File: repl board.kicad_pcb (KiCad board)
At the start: 2 copper layers, 55.5 x 32.2 mm, 24 parts, among them IC1 SN74HC42D, IC2 SN74HC42D, J2 Conn_01x16, J3 Conn_01x16, SW2 SW_Reed, U1 ATmega32U2-AU, Y1 ABM8G-16.000MHZ-4Y-T3

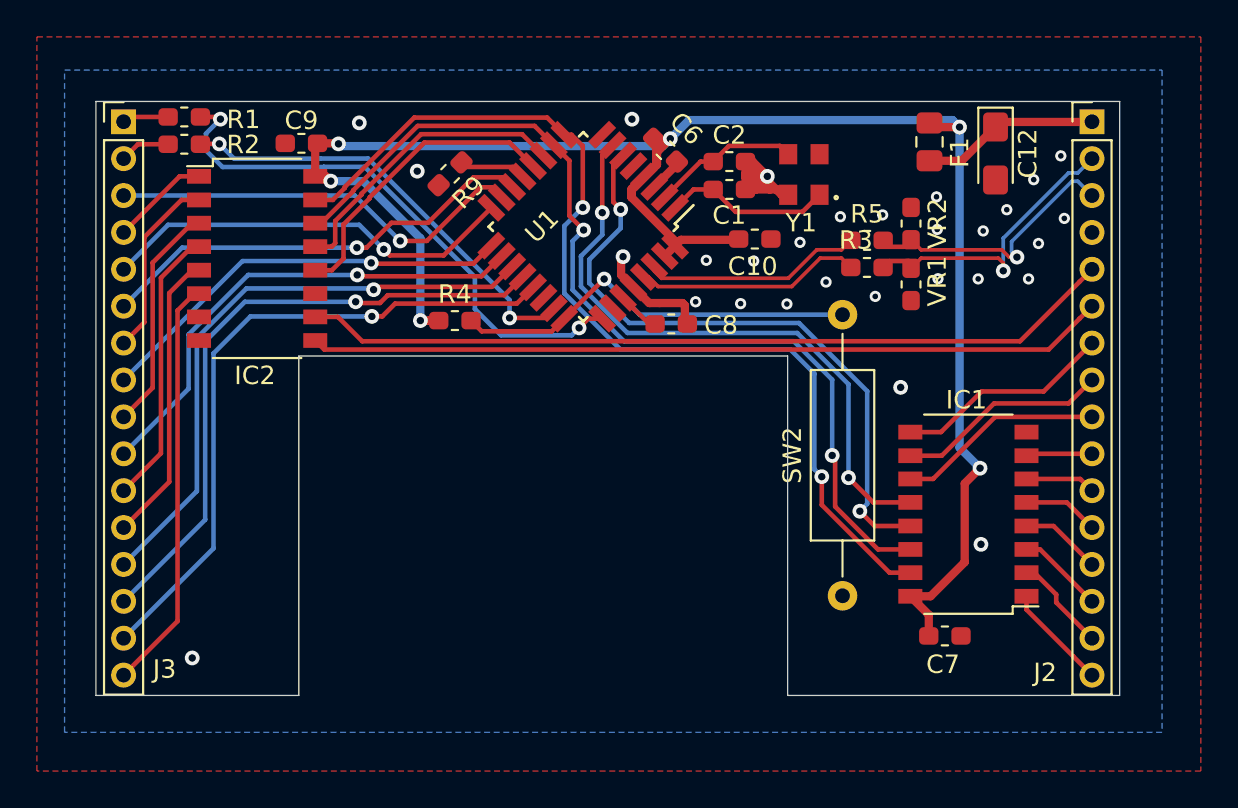
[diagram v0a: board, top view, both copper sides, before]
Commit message: Fix chrystal
Fix Chrystal footprint, added ICSP header
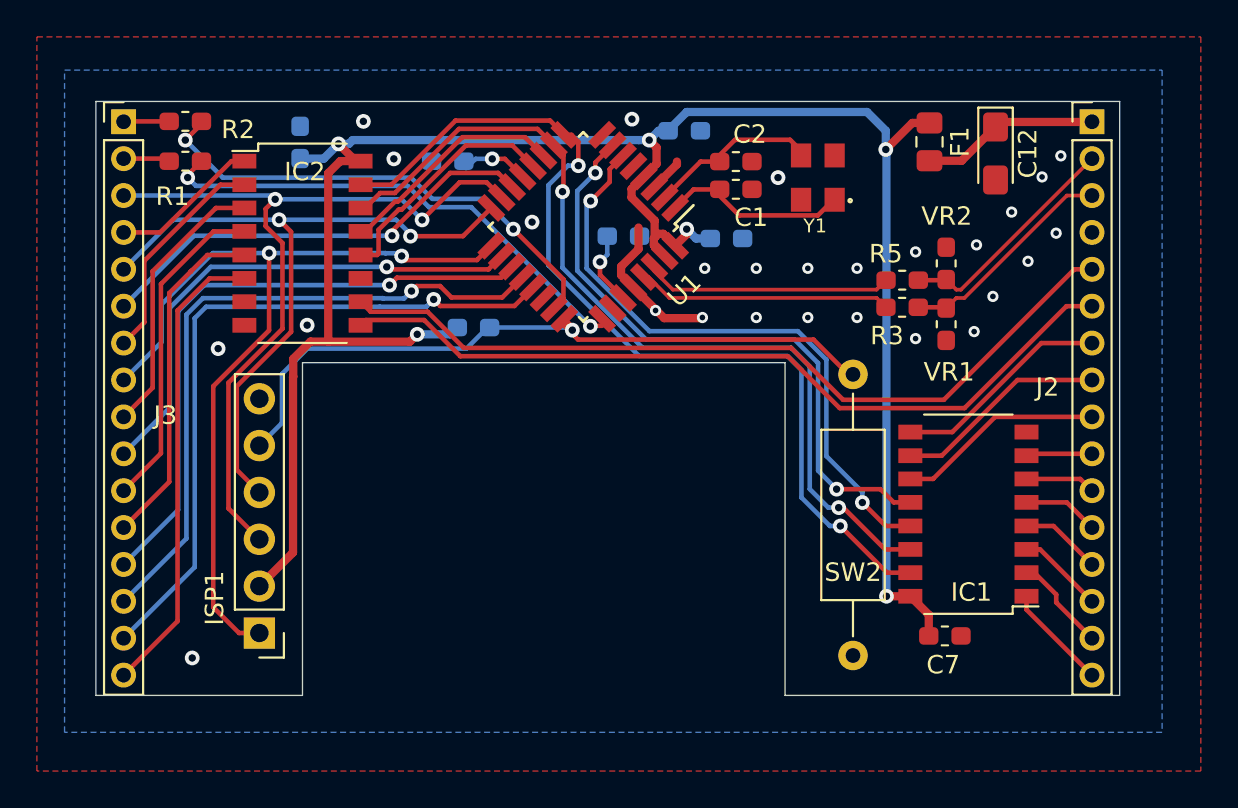
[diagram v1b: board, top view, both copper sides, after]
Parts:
- added ISP1: AVR-ISP-6, Connector_PinHeader_2.54mm:PinHeader_1x06_P2.54mm_Vertical, F.Cu at (172.2, 109.0)
- C10, C6, C8, C9, R4, R9: moved to B.Cu
- Y1: value ABM8G-16.000MHZ-4Y-T3 -> ABM8G-16MHZ-4Y-T3
- moved C8 5.42 mm to (191.9, 87.5)
- moved SW2 3.29 mm to (204.3, 110.2)
- moved VR2 2.88 mm to (209.4, 89.0)
- moved R3 2.88 mm to (207.0, 91.4)
- moved R5 2.88 mm to (207.0, 89.9)
- moved VR1 2.88 mm to (209.4, 92.3)
- moved IC2 2.59 mm to (174.5, 87.9)
- moved R1 2.40 mm to (168.1, 83.4)
- moved C10 1.54 mm to (197.5, 87.6)
- moved C6 1.46 mm to (195.2, 81.8), turned to 0 degrees
- moved R2 1.24 mm to (168.1, 81.3)
- moved R4 1.08 mm to (183.8, 92.5)
- moved Y1 0.78 mm to (202.4, 84.3)
- moved R9 0.69 mm to (182.4, 83.4), turned to 180 degrees
- moved C1 0.35 mm to (198.0, 85.0)
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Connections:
- net Net-(R4-Pad2) renamed Reset
- J2 pad 2: D+ -> D-
- J2 pad 3: D- -> D+
- J3 pad 1: CAP -> SCR
- J3 pad 2: SCR -> CAP
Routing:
- net COL3: track 23.1 -> 48.0 mm, vias 1 -> 2
- net COL1: track 23.0 -> 43.2 mm, vias 1 -> 2
- net Reset: track 22.4 -> 39.6 mm
- net COL2: track 22.7 -> 38.9 mm, vias 1 -> 2
- net VCC: track 99.8 -> 112.8 mm
- net GND: track 20.8 -> 10.1 mm, vias 29 -> 27
- net D+: track 16.1 -> 12.0 mm, vias 1 -> 0
- net ROWB: track 52.4 -> 48.6 mm
- net ROWE: track 16.1 -> 12.4 mm
- net ROWF: track 16.3 -> 13.0 mm
- net /LED_CAP: track 30.2 -> 27.0 mm
- net /LED_SCR: track 23.9 -> 26.8 mm
- net ROW14: track 15.9 -> 18.8 mm
- net ROW15: track 22.5 -> 25.3 mm
- net ROW10: track 5.35 -> 8.15 mm
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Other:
- outline, holes or cut-outs redrawn

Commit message: v1.05
Corrected USB D+/D-
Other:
- board text added: "Filco TKL Controller v1.05 2020 Markus Knutsson CERN-OHL-S v2+ github.com/TweetyDaBird/"
- board text removed: "2020 Markus Knutsson CERN-OHL-S v2+ github.com/TweetyDaBird/"

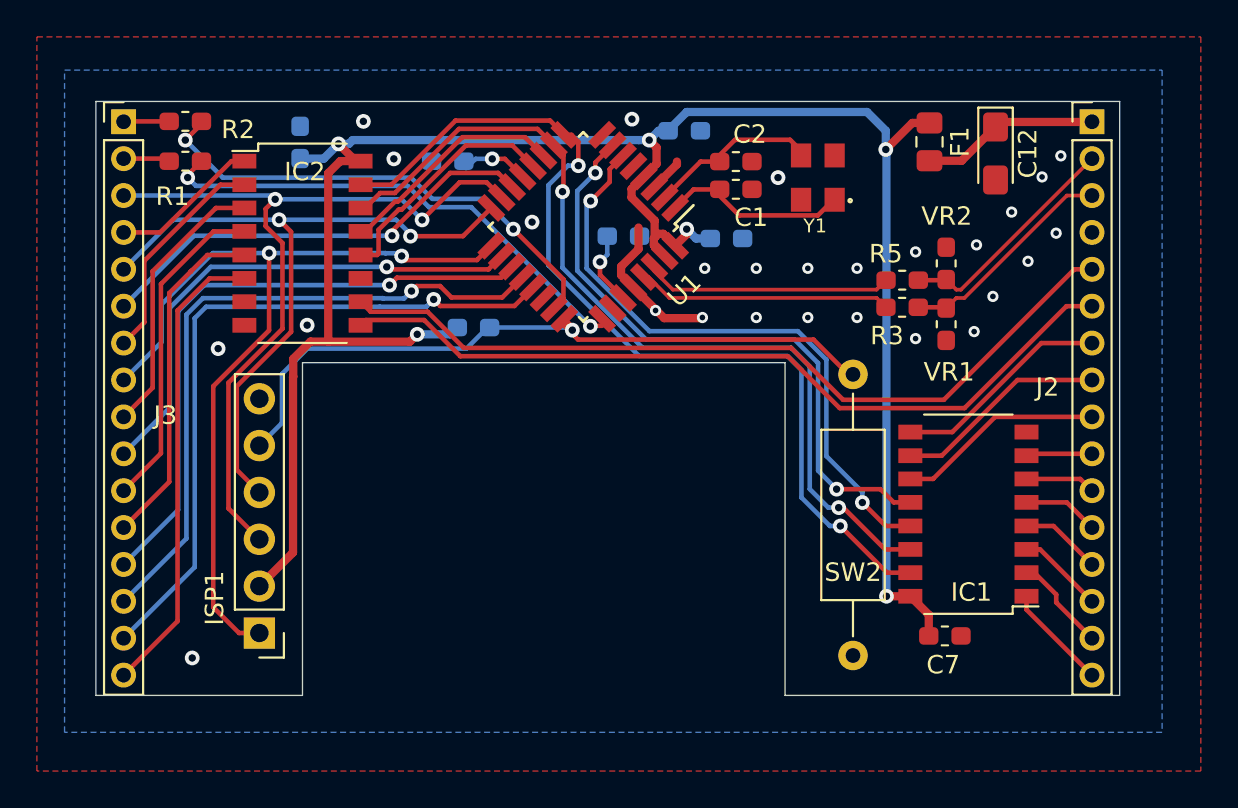
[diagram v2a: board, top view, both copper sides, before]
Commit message: Adjustment for DRC
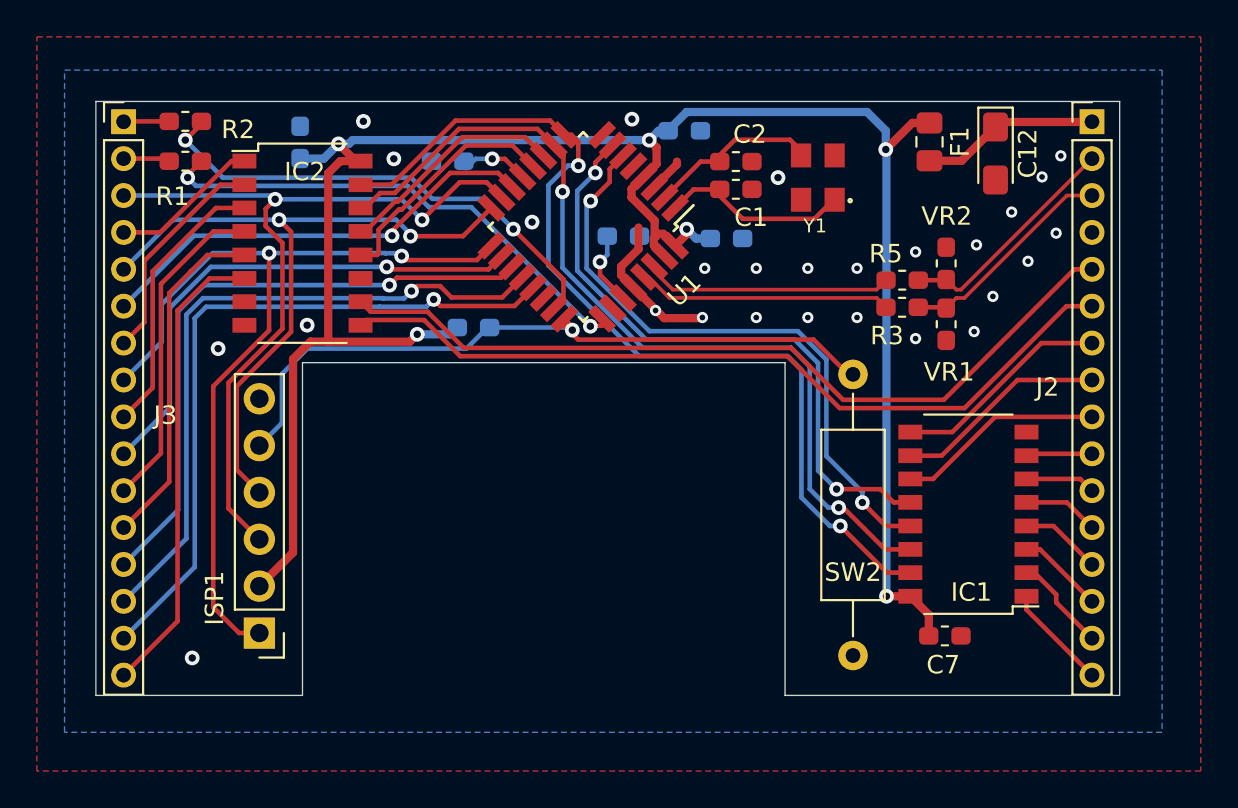
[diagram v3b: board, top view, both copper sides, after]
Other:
- rule via_min_size: 0.4 -> 0.6
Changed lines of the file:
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@@
     (thickness 1.6)
     (drawings 9)
-    (tracks 428)
+    (tracks 426)
     (zones 0)
     (modules 25)
@@
     (via_size 0.8)
     (via_drill 0.4)
-    (via_min_size 0.4)
+    (via_min_size 0.6)
     (via_min_drill 0.3)
     (user_via 0.6096 0.3048)
@@
     (pad_to_mask_clearance 0.051)
     (solder_mask_min_width 0.25)
-    (aux_axis_origin 0 0)
+    (aux_axis_origin 163.3 112.4)
     (visible_elements 7FFFFFFF)
     (pcbplotparams
-      (layerselection 0x010fc_ffffffff)
+      (layerselection 0x010f0_ffffffff)
       (usegerberextensions false)
       (usegerberattributes false)
@@
       (viasonmask false)
       (mode 1)
-      (useauxorigin false)
+      (useauxorigin true)
       (hpglpennumber 1)
       (hpglpenspeed 20)
@@
       (outputformat 1)
       (mirror false)
-      (drillshape 1)
+      (drillshape 0)
       (scaleselection 1)
-      (outputdirectory ""))
+      (outputdirectory "gerber/"))
   )
   (net 0 "")
@@
     (descr "32-Lead Plastic Thin Quad Flatpack (PT) - 7x7x1.0 mm Body, 2.00 mm [TQFP] (see Microchip Packaging Specification 00000049BS.pdf)")
     (tags "QFP 0.8")
+    (clearance 0.2)
     (attr smd)
     (fp_text reference U1 (at -1.449981 -6.299319 45) (layer F.SilkS)
@@
   (segment (start 194.106731 91.948) (end 196.088 91.948) (width 0.45) (layer F.Cu) (net 1))
   (via (at 179.451 83.312) (size 0.8) (drill 0.4) (layers F.Cu B.Cu) (net 1))
-  (segment (start 198.173 86.378) (end 202.438 86.378) (width 0.25) (layer F.Cu) (net 2) (status 20))
-  (segment (start 196.765 84.97) (end 198.173 86.378) (width 0.25) (layer F.Cu) (net 2) (status 10))
-  (segment (start 195.704215 84.97) (end 194.70452 85.969695) (width 0.25) (layer F.Cu) (net 2) (status 20))
-  (segment (start 196.765 84.97) (end 195.704215 84.97) (width 0.25) (layer F.Cu) (net 2) (status 10))
-  (segment (start 203.288 85.528) (end 202.438 86.378) (width 0.25) (layer F.Cu) (net 2))
-  (segment (start 203.348 85.528) (end 203.288 85.528) (width 0.25) (layer F.Cu) (net 2))
+  (segment (start 195.704215 84.97) (end 196.765 84.97) (width 0.25) (layer F.Cu) (net 2))
+  (segment (start 194.70452 85.969695) (end 195.704215 84.97) (width 0.25) (layer F.Cu) (net 2))
+  (segment (start 202.2528 86.5632) (end 203.288 85.528) (width 0.25) (layer F.Cu) (net 2))
+  (segment (start 203.288 85.528) (end 203.348 85.528) (width 0.25) (layer F.Cu) (net 2))
+  (segment (start 196.765 84.97) (end 198.3582 86.5632) (width 0.25) (layer F.Cu) (net 2))
+  (segment (start 198.3582 86.5632) (end 202.2528 86.5632) (width 0.25) (layer F.Cu) (net 2))
   (segment (start 197.947 82.278) (end 196.765 83.46) (width 0.25) (layer F.Cu) (net 3) (status 20))
   (segment (start 196.082844 83.46) (end 194.138834 85.40401) (width 0.25) (layer F.Cu) (net 3) (status 20))
@@
   (segment (start 175.895 93.218) (end 175.900989 93.223989) (width 0.45) (layer F.Cu) (net 4))
   (via (at 180.721 92.82399) (size 0.8) (drill 0.4) (layers F.Cu B.Cu) (net 4))
-  (segment (start 173.986212 104.651788) (end 172.1612 106.4768) (width 0.45) (layer F.Cu) (net 4))
-  (segment (start 174.93388 93.218) (end 173.99799 94.15389) (width 0.45) (layer F.Cu) (net 4))
-  (segment (start 175.895 93.218) (end 174.93388 93.218) (width 0.45) (layer F.Cu) (net 4))
-  (segment (start 173.99799 94.15389) (end 173.99799 95.11501) (width 0.45) (layer F.Cu) (net 4))
-  (segment (start 173.99799 95.11501) (end 173.986212 95.126788) (width 0.45) (layer F.Cu) (net 4))
-  (segment (start 173.986212 95.126788) (end 173.986212 104.651788) (width 0.45) (layer F.Cu) (net 4))
   (segment (start 206.12102 81.78802) (end 206.12102 82.804) (width 0.45) (layer B.Cu) (net 4))
   (segment (start 193.802 81.788) (end 194.31 81.788) (width 0.45) (layer B.Cu) (net 4))
@@
   (segment (start 205.105 80.772) (end 206.12102 81.78802) (width 0.45) (layer B.Cu) (net 4))
   (segment (start 195.326 80.772) (end 205.105 80.772) (width 0.45) (layer B.Cu) (net 4))
+  (segment (start 173.986212 94.165668) (end 173.986212 104.651788) (width 0.45) (layer F.Cu) (net 4))
+  (segment (start 173.986212 104.651788) (end 172.1612 106.4768) (width 0.45) (layer F.Cu) (net 4))
+  (segment (start 175.895 93.218) (end 174.93388 93.218) (width 0.45) (layer F.Cu) (net 4))
+  (segment (start 174.93388 93.218) (end 173.986212 94.165668) (width 0.45) (layer F.Cu) (net 4))
   (segment (start 190.627 89.599639) (end 190.627 88.9) (width 0.25) (layer F.Cu) (net 5))
   (segment (start 191.876093 90.848732) (end 190.627 89.599639) (width 0.25) (layer F.Cu) (net 5))
